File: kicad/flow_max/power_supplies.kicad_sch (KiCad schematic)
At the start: 14 parts, among them U14 LM66100DCKR, U2 MIC5504-1.8YMT, U3 MPM3811GG-Z

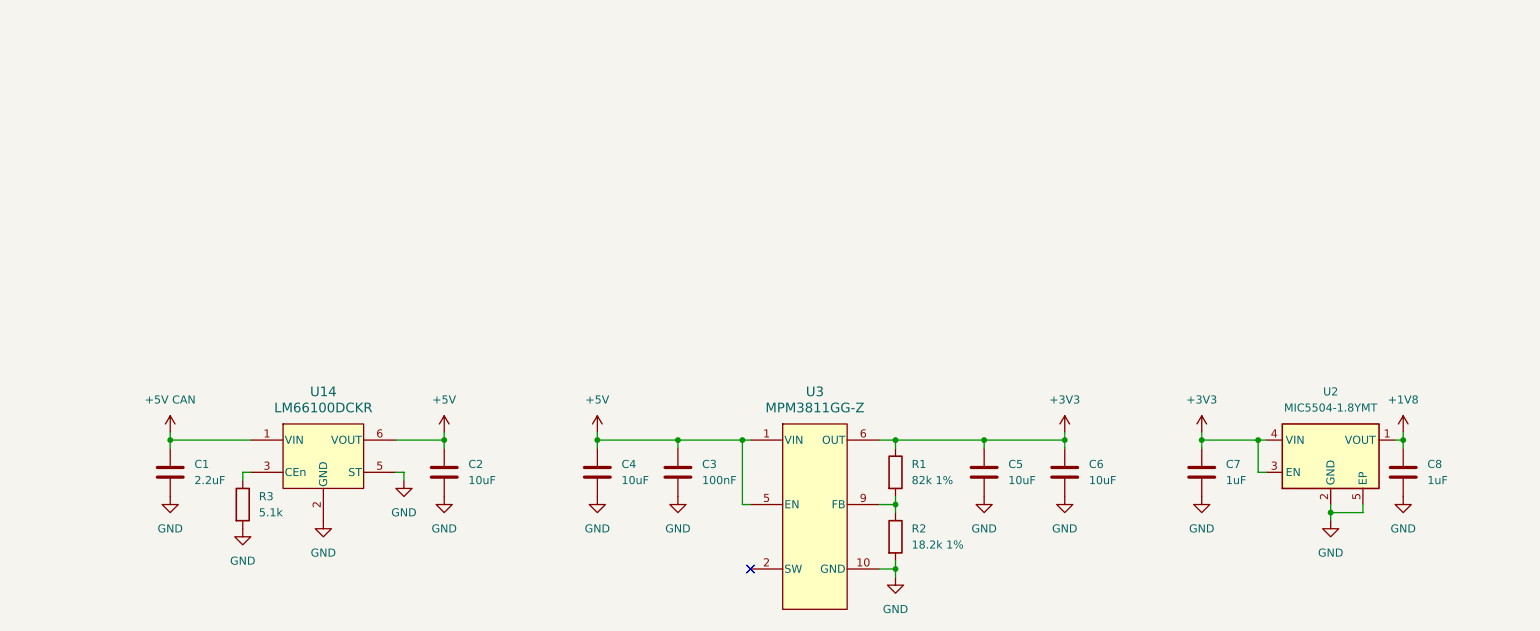
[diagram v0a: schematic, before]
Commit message: Added in the schematic common mode choke filters and TVS diodes to parts where it is needed. Made the polarity protection circuit in schematic. Put placeholders for power supply regulators in schematic.
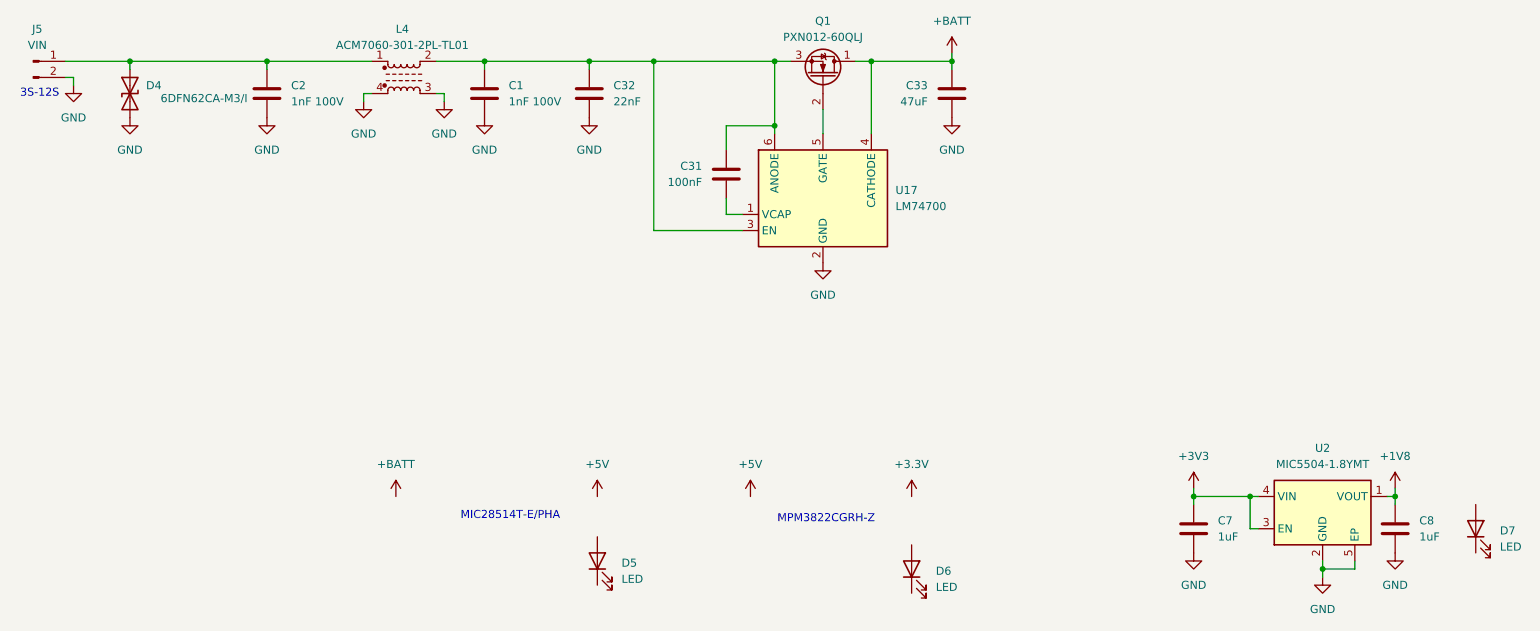
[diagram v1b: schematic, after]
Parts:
- removed C3: 100nF, symbol Device:C
- removed C4, C5, C6: 10uF, symbol Device:C
- removed R1: 82k 1%, symbol Device:R
- removed R2: 18.2k 1%, symbol Device:R
- removed R3: 5.1k, symbol Device:R
- removed U14: LM66100DCKR, Power:LM66100DCKR, symbol Power:LM66100DCKR
- removed U3: MPM3811GG-Z, Power:QFN2x2x1p6_MPM3811_MNP, symbol Power:MPM3811GG-Z
- added C31: 100nF, symbol Device:C
- added C32: 22nF, symbol Device:C
- added C33: 47uF, symbol Device:C
- added D4: 6DFN62CA-M3/I, symbol Device:D_TVS
- added D5, D6, D7: LED, symbol Device:LED
- added J5: VIN, symbol Connector:Conn_01x02_Pin
- added L4: ACM7060-301-2PL-TL01, symbol Device:L_Ferrite_Coupled_1243
- added Q1: PXN012-60QLJ, symbol Device:Q_NMOS_Depletion_DGS
- added U17: LM74700, Package_TO_SOT_SMD:SOT-23-6, symbol Power_Management:LM74700
- C1: value 2.2uF -> 1nF 100V
- C2: value 10uF -> 1nF 100V
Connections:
- net +5V CAN is gone; now on net GND: C1.1
- net +5V: no longer C2.1
- net GND: now also C2.1, C32.1, C33.1, D4.2 (A2), J5.2 (Pin_2), L4.3, L4.4, U17.2 (GND); no longer C1.2, C2.2
- new net: C1.2, C31.2, C32.2, L4.2, Q1.3 (S), U17.3 (EN), U17.6 (ANODE)
- new net: C31.1, U17.1 (VCAP)
- new net: C2.2, D4.1 (A1), J5.1 (Pin_1), L4.1
- new net: Q1.2 (G), U17.5 (GATE)
- new net +BATT: C33.2, Q1.1 (D), U17.4 (CATHODE)
- no-connect marks 1 -> 0
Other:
- note added: "3S-12S"
- note added: "MIC28514T-E/PHA"
- note added: "MPM3822CGRH-Z"
- moved on the sheet: C7, C8, U2
